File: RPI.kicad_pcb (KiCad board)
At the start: 2 copper layers, 65 x 56 mm, 38 parts, among them J1 Conn_01x02_Male, J2 GPIO, J5 Conn_01x06, J6 Conn_01x04, J7 Conn_01x03, J8 Conn_01x02, J9 Conn_01x02, Q1 IRF9540N, Q2 IRF9540N, Q3 BC856BDW1, SW1 SW_SPDT, SW2 SW_SPDT, U1 LM1085-ADJ

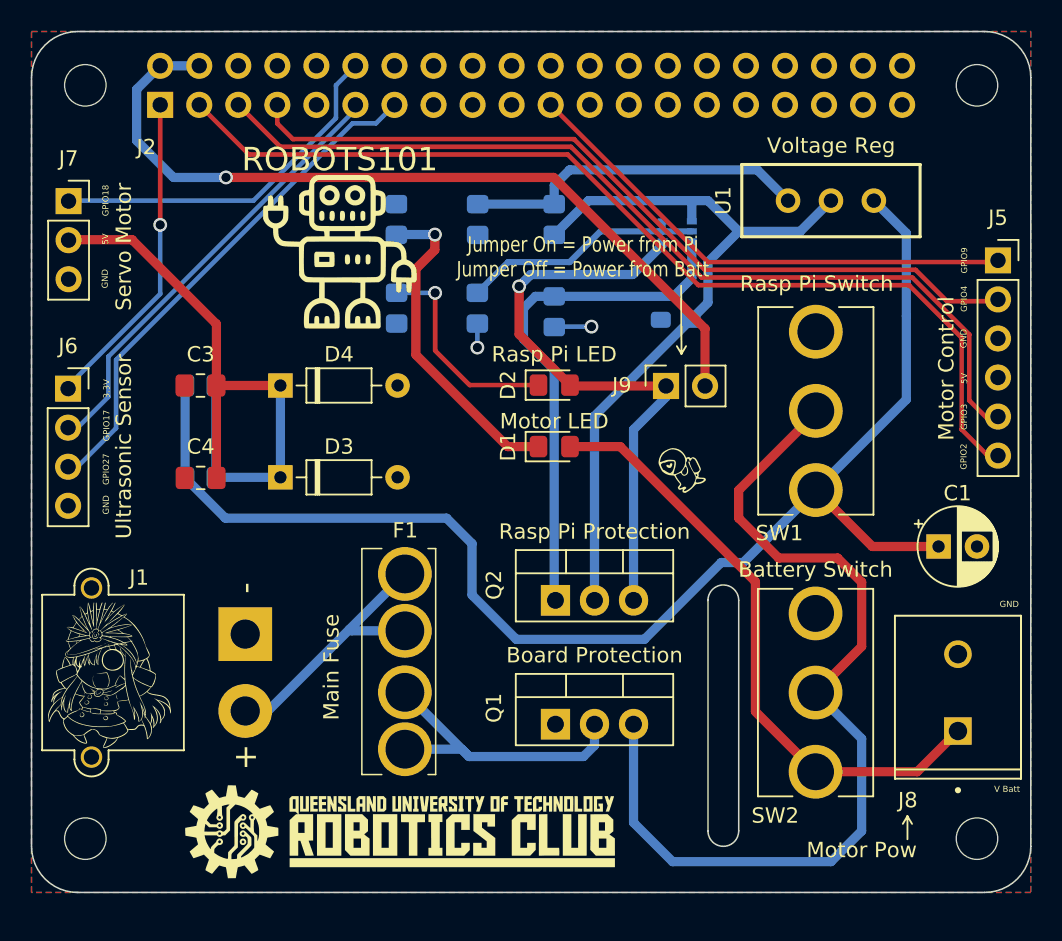
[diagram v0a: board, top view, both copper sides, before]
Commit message: Changed regulator
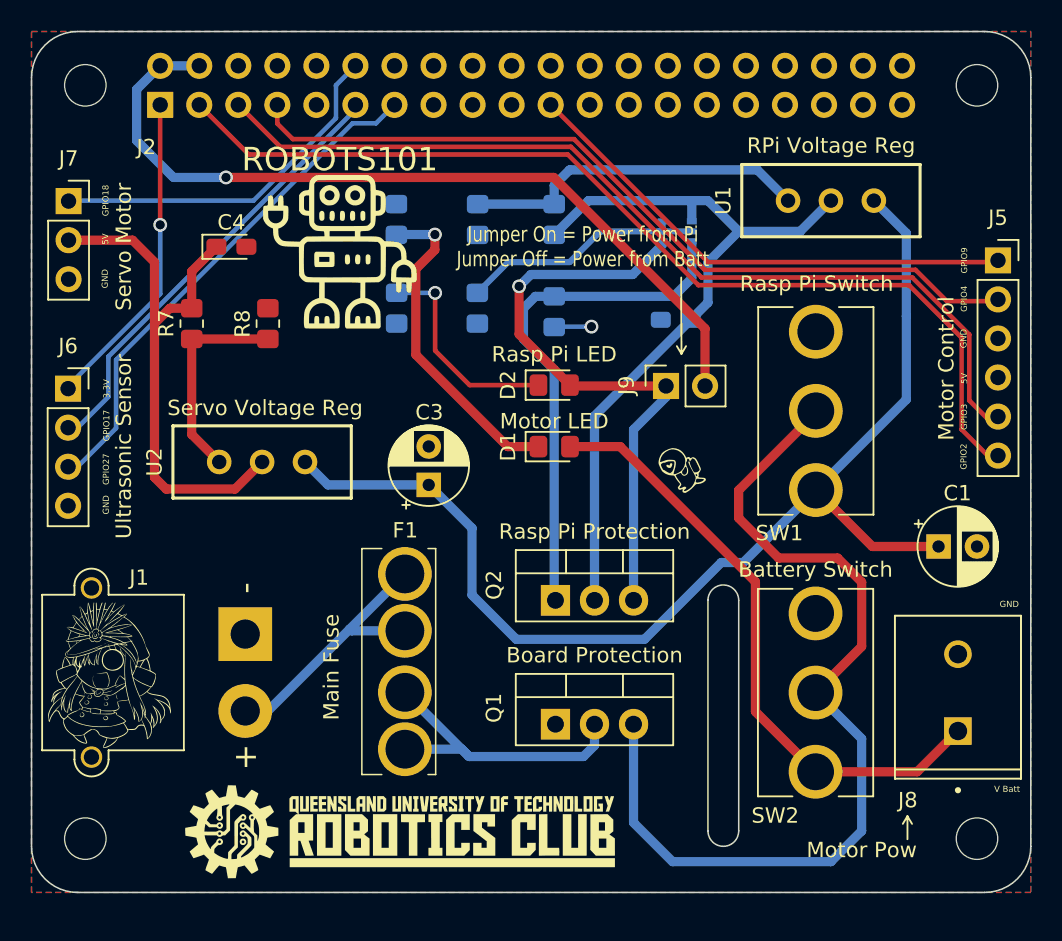
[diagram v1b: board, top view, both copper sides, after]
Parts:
- removed D3, D4: 1N52318, Diode_THT:D_DO-35_SOD27_P7.62mm_Horizontal
- added U2: LM1085-ADJ, RPi_Hat:LM1085-5.0, F.Cu at (115.0, 72.0)
- C3: value 10nF -> 10u; footprint Capacitor_SMD:C_0805_2012Metric_Pad1.18x1.45mm_HandSolder -> Capacitor_THT:CP_Radial_D5.0mm_P2.50mm
- C4: value 10uF -> 100u; footprint Capacitor_SMD:C_0805_2012Metric_Pad1.18x1.45mm_HandSolder -> Capacitor_Tantalum_SMD:CP_EIA-2012-12_Kemet-R_Pad1.30x1.05mm_HandSolder
- R7: value 3.3 -> 121; moved to F.Cu
- R8: value 3.3 -> 365; moved to F.Cu
- moved C3 16.2 mm to (125.8, 73.5), turned to 90 degrees
- moved C4 15.2 mm to (113.0, 58.0), turned to 0 degrees
- moved R8 10.9 mm to (115.4, 63.0), turned to 90 degrees
- moved R7 4.07 mm to (110.4, 63.0), turned to -90 degrees
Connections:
- C3 pad 1: Vdrive -> VCC
- R7 pad 1: VCC -> Vdrive
- R7 pad 2: Vdrive -> Net-(R7-Pad2)
- R8 pad 1: VCC -> Net-(R7-Pad2)
- R8 pad 2: Vdrive -> GND
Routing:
- net Net-(R7-Pad2): track 0.00 -> 13.7 mm
- net VCC: track 90.6 -> 77.9 mm
- net Vdrive: track 41.6 -> 35.7 mm
- net GND: track 3.99 -> 2.43 mm, vias 2 -> 1
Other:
- board text added: "RPi Voltage Reg"
- board text added: "Servo Voltage Reg"
- board text removed: "Voltage Reg"

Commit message: V2 Ready for checking
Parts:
- removed the G at (105.1, 85.9)
- removed Q3: BC856BDW1, Package_TO_SOT_SMD:SOT-363_SC-70-6
- added Q4: DMMT5401-7-F, RPi_Hat:SOT95P285X140-6N, F.Cu at (127.2, 61.9)
- C2, R1, R2, R3, R4, R5, R6: moved to F.Cu
- U1, U2: footprint RPi_Hat:LM1085-5.0 -> Package_TO_SOT_THT:TO-220-3_Vertical
- moved U2 41.8 mm to (154.0, 57.0), turned to -90 degrees
- moved SW2 39.6 mm to (114.0, 73.0), turned to 180 degrees
- moved R3 37.4 mm to (109.9, 91.0), turned to 0 degrees
- moved ROBOTS101 31.6 mm to (131.0, 88.0)
- moved C3 30.4 mm to (150.0, 92.0), turned to 0 degrees
- moved R4 28.5 mm to (110.0, 87.0), turned to 180 degrees
- moved D1 27.1 mm to (115.7, 91.0)
- moved D2 27.0 mm to (115.8, 87.0)
- moved Q2 26.8 mm to (146.1, 57.0), turned to -90 degrees
- moved J1 26.3 mm to (113.7, 56.9)
- moved R7 25.6 mm to (135.0, 56.0), turned to 90 degrees
- moved Q1 23.3 mm to (146.0, 69.0), turned to -90 degrees
- moved J9 22.3 mm to (162.8, 61.4), turned to 180 degrees
- moved C2 22.0 mm to (120.3, 58.5)
- moved SW1 21.5 mm to (130.0, 73.0), turned to 180 degrees
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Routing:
- net VD: track 39.3 -> 97.2 mm, vias 1 -> 2
- net Vdrive: track 35.7 -> 68.0 mm, vias 0 -> 2
- net +BATT: track 40.0 -> 69.9 mm, vias 0 -> 1
- net /GPIO4/GPCLK: track 52.9 -> 80.6 mm
- net VCC: track 77.9 -> 50.9 mm, vias 0 -> 1
- net Net-(Q1-Pad3): track 60.6 -> 36.5 mm
- net Net-(R1-Pad2): track 22.7 -> 45.0 mm, vias 0 -> 2
- net /GPIO17/GEN0: track 28.4 -> 47.4 mm, vias 0 -> 1
- net Net-(F1-Pad3): track 20.1 -> 38.8 mm
- net Net-(D1-Pad1): track 21.3 -> 3.77 mm, vias 1 -> 0
- net /GPIO27/GEN2: track 32.9 -> 50.1 mm, vias 0 -> 1
- net /GPIO3/SCL1: track 60.3 -> 76.3 mm
- net +3V3: track 20.9 -> 36.1 mm, vias 1 -> 0
- net /GPIO18/GEN1: track 23.0 -> 37.3 mm
- net +5V: track 53.8 -> 66.5 mm, vias 1 -> 2
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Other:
- board text added: "Battery Power"
- board text added: "J9 on to power pi from battery J9 off to power pi from microUSB"
- board text added: "Motor Power"
- board text added: "Robots101 PiHat V2"
- board text added: "SW1 LED"
- board text added: "SW2 LED"
- board text added: "Servo"
- board text removed: "Battery Switch"
- board text removed: "Board Protection"
- board text removed: "Jumper On = Power from Pi Jumper Off = Power from Batt"
- board text removed: "Motor LED"
- board text removed: "Motor Pow"
- board text removed: "Rasp Pi LED"
- board text removed: "Rasp Pi Protection"
- board text removed: "Rasp Pi Switch"
- board text removed: "Servo Motor"
- board text removed: "Servo Voltage Reg"

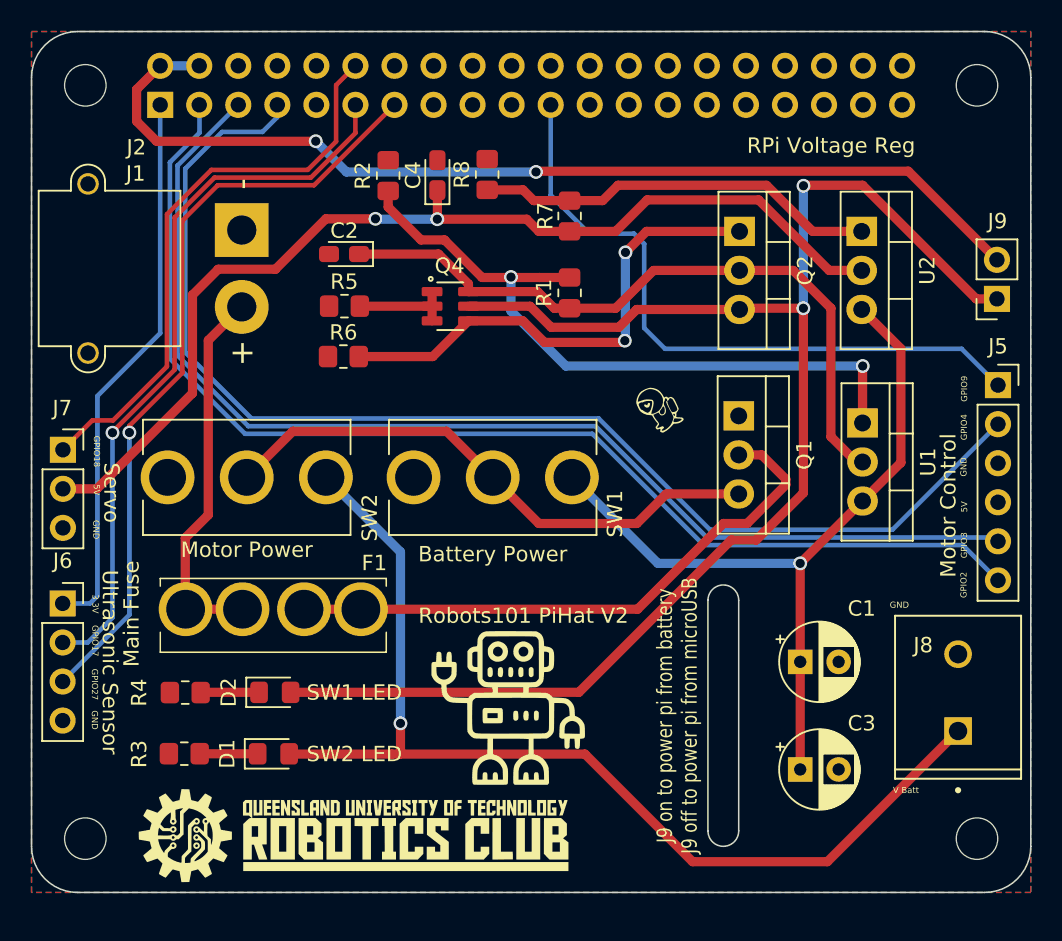
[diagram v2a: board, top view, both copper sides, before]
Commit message: V2 update with THT copper shapes and info given
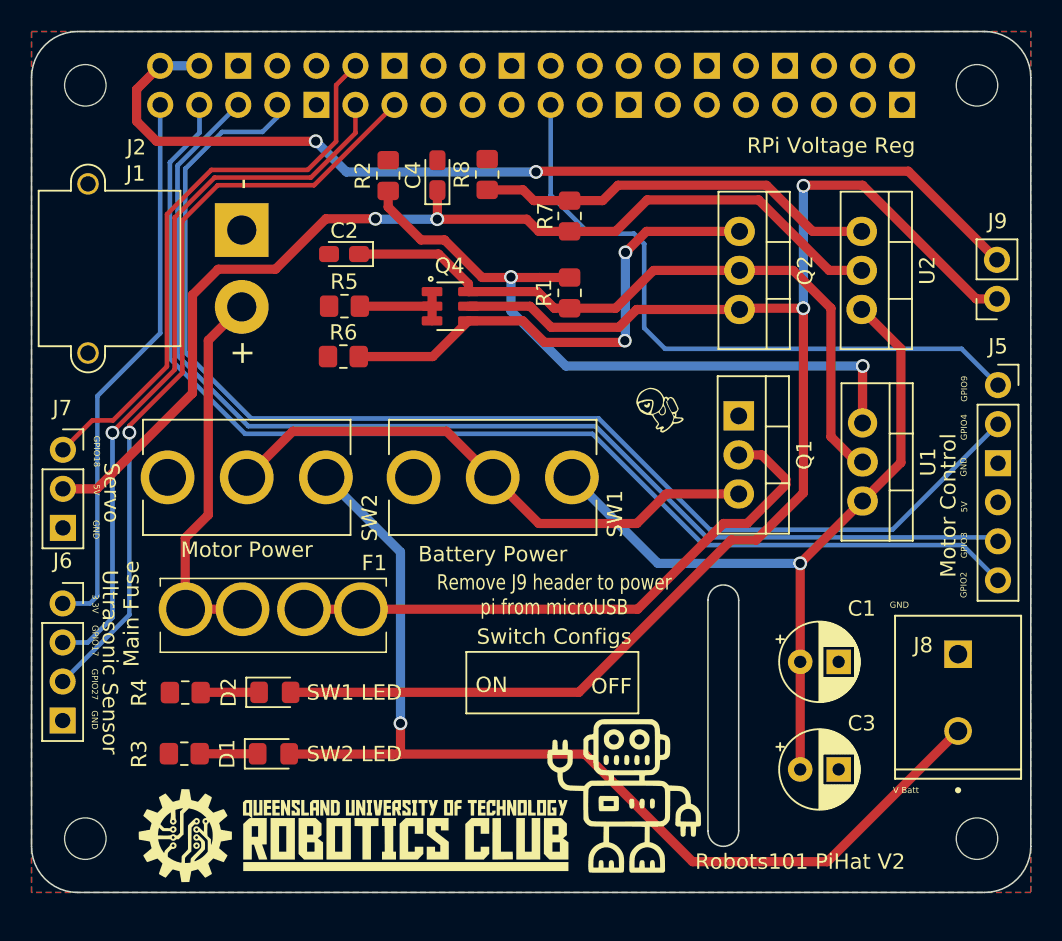
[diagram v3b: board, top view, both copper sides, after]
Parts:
- moved ROBOTS101 9.47 mm to (138.5, 93.7)
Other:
- board text added: "OFF"
- board text added: "ON"
- board text added: "Remove J9 header to power pi from microUSB"
- board text added: "Switch Configs"
- board text removed: "J9 on to power pi from battery J9 off to power pi from microUSB"
